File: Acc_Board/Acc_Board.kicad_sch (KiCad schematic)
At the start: 44 parts, among them J1 1053091202, J10 1053091202, J11 1053091202, J12 776087-1, J2 1053091202, J3 1053091202, J4 1053091202, J5 1053091202, J6 1053091202, J9 1053091202, K1 Relay_SPST-NO, U1 ISO1050DUB, U13 R-78B5.0-2.0, U2 NUCLEO-L432KC, U4 PQDE6W-Q110-S5-H-D

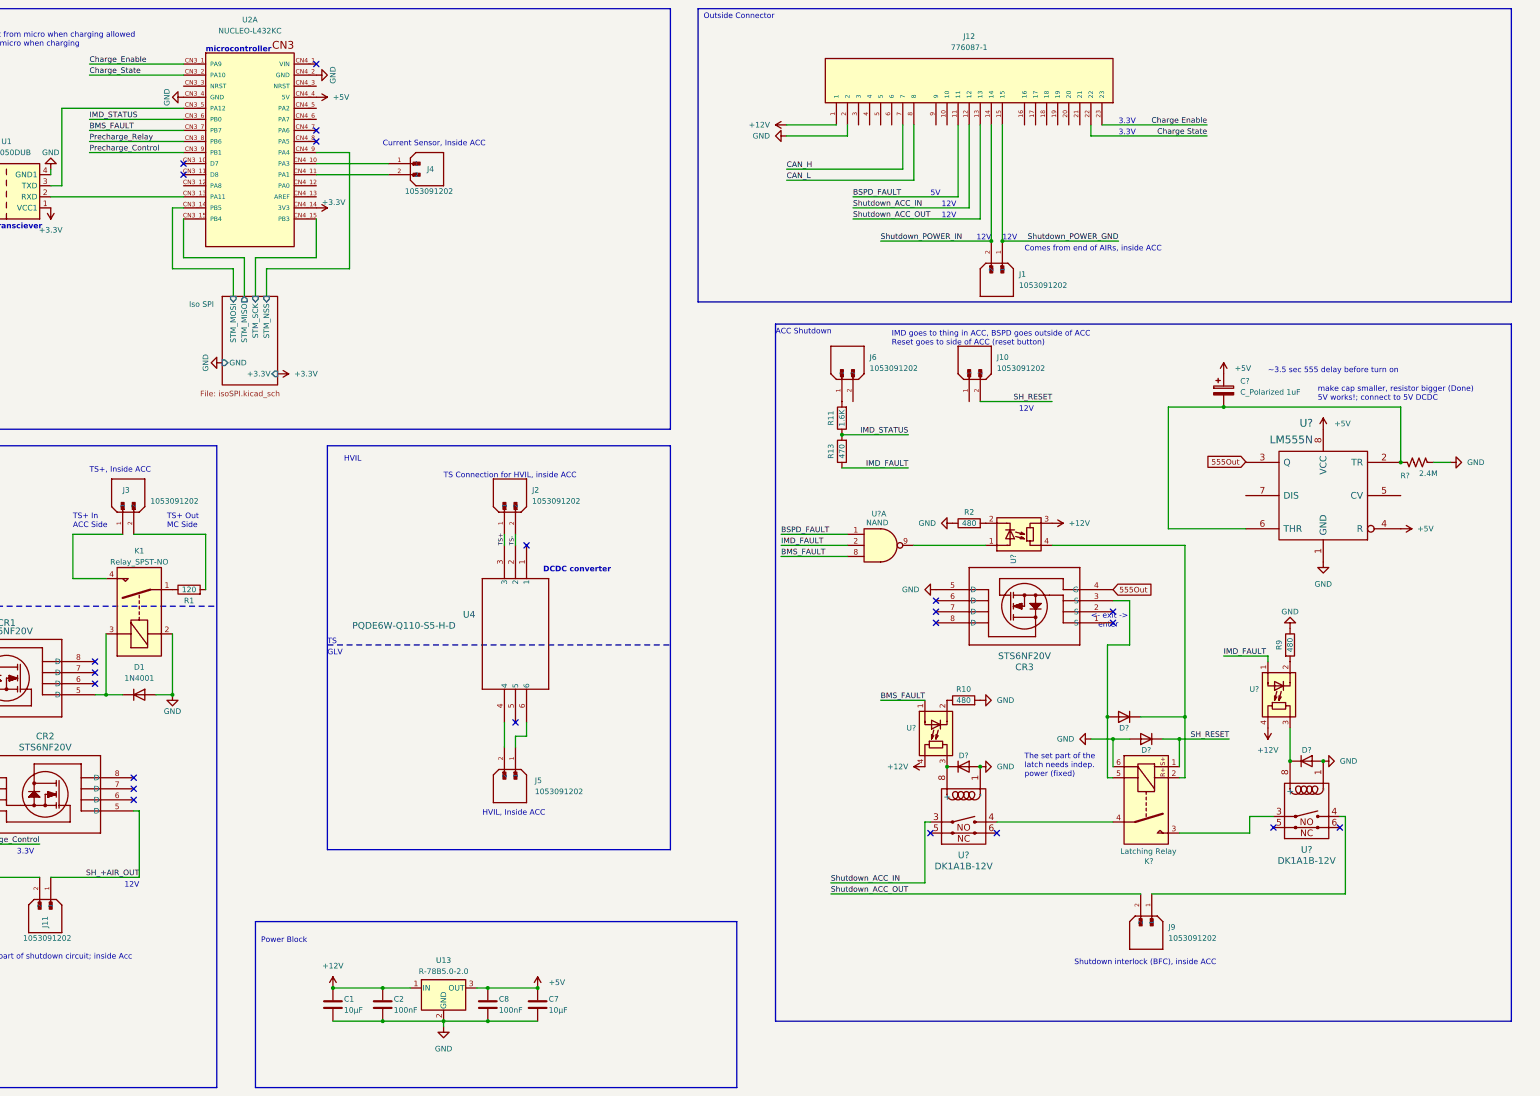
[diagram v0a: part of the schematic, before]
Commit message: Updated shutdown circuit pins in acc board
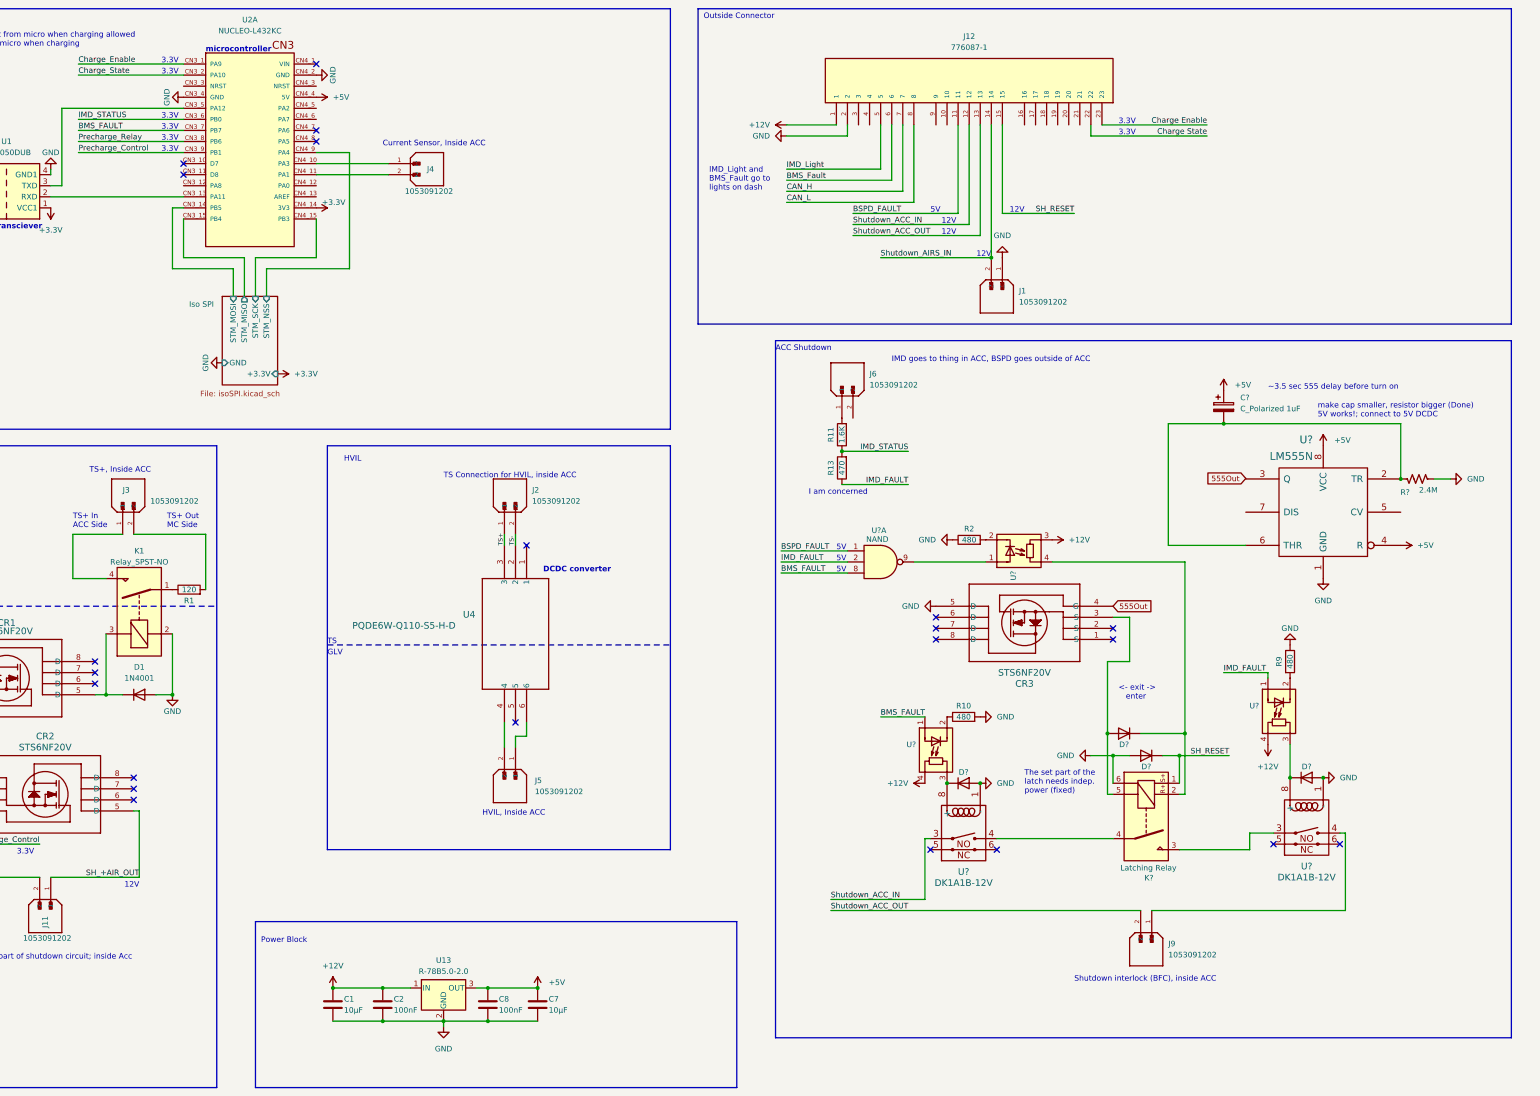
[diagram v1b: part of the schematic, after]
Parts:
- removed J10: 1053091202, 1FS_2_Global_Footprint_Library:MOLEX_1053091202, symbol molex_1053091202:1053091202
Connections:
- net GND: now also J1.1
- net SH_RESET: now also J12.15
- net IMD_Light: now reaches J12.5
- net BMS_Fault: now reaches J12.6
- removed net Shutdown_POWER_GND: J1.1, J12.15
- net Shutdown_POWER_IN renamed Shutdown_AIRS_IN
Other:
- note added: "I am concerned"
- note added: "IMD goes to thing in ACC, BSPD goes outside of ACC"
- note added: "IMD_Light and BMS_Fault go to lights on dash"
- note removed: "Comes from end of AIRs, inside ACC"
- note removed: "IMD goes to thing in ACC, BSPD goes outside of ACC Reset goes to side of ACC (reset button)"
- moved on the sheet: C?, CR3, D?, J1, J6, J9, K?, R10, R11, R13, R2, R9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

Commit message: Worked on Acc Board tracks
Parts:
- C?: value C_Polarized 1uF -> 1µF; footprint Capacitor_THT:CP_Axial_L20.0mm_D10.0mm_P26.00mm_Horizontal -> (none)
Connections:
- net CAN_H: now also J12.8; no longer J12.7
- net CAN_L: now also J12.7; no longer J12.8
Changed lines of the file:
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@@
     (effects (font (size 1.27 1.27)) (justify left bottom))
   )
-  (text "~3.5 sec 555 delay before turn on" (at 345.44 102.87 0)
+  (text "~3.5 sec 555 delay before turn on" (at 342.9 102.87 0)
     (effects (font (size 1.27 1.27)) (justify left bottom))
   )
@@
     (effects (font (size 1.27 1.27)) (justify left bottom))
   )
-  (label "CAN_L" (at 234.95 59.69 0) (fields_autoplaced)
+  (label "CAN_H" (at 234.95 59.69 0) (fields_autoplaced)
     (effects (font (size 1.27 1.27)) (justify left bottom))
   )
@@
     (effects (font (size 1 1)) (justify left bottom))
   )
-  (label "CAN_H" (at 234.95 57.15 0) (fields_autoplaced)
-    (effects (font (size 1.27 1.27)) (justify left bottom))
-  )
   (label "Precharge_Control" (at 63.5 207.01 180) (fields_autoplaced)
     (effects (font (size 1.27 1.27)) (justify right bottom))
   )
   (label "BSPD_FAULT" (at 233.68 139.7 0) (fields_autoplaced)
+    (effects (font (size 1.27 1.27)) (justify left bottom))
+  )
+  (label "CAN_L" (at 234.95 57.15 0) (fields_autoplaced)
     (effects (font (size 1.27 1.27)) (justify left bottom))
   )
@@
       (effects (font (size 1.27 1.27)) (justify left))
     )
-    (property "Value" "C_Polarized 1uF" (at 339.09 107.061 0)
-      (effects (font (size 1.27 1.27)) (justify left))
-    )
-    (property "Footprint" "Capacitor_THT:CP_Axial_L20.0mm_D10.0mm_P26.00mm_Horizontal" (at 336.2452 110.49 0)
-      (effects (font (size 1.27 1.27)) hide)
-    )
+    (property "Value" "1µF" (at 339.09 107.061 0)
+      (effects (font (size 1.27 1.27)) (justify left))
+    )
+    (property "Footprint" "" (at 336.2452 110.49 0)
+      (effects (font (size 1.27 1.27)) hide)
+    )

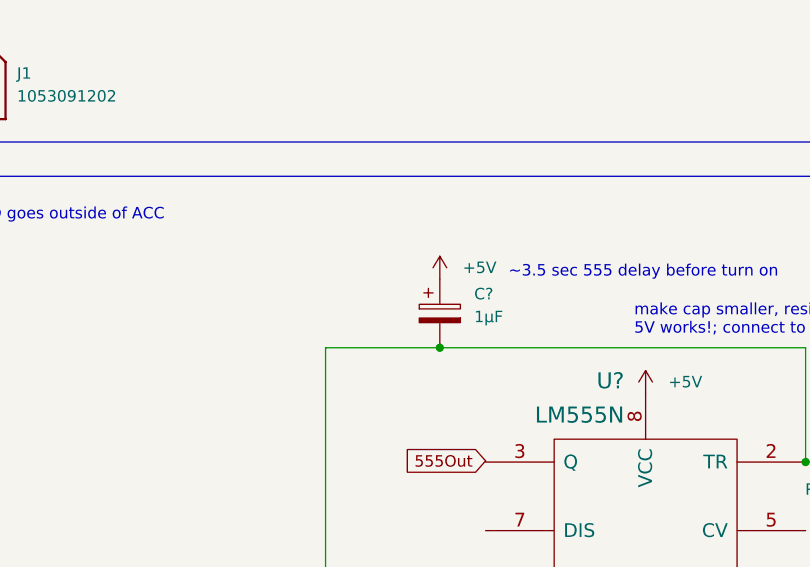
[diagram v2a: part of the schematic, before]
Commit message: fixed 555 capacitors
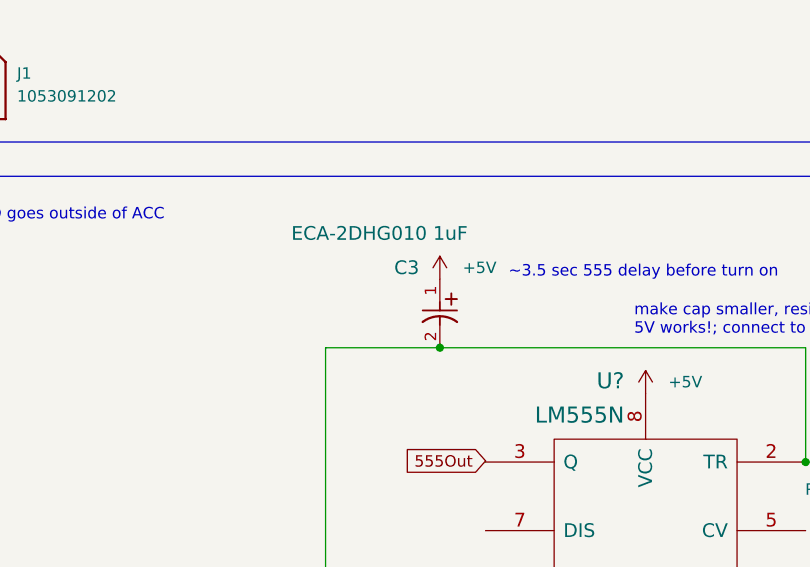
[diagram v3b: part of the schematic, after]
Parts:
- removed C?: 1µF, symbol Device:C_Polarized
- added C3: ECA-2DHG010 1uF, PCAP_63x112_PAN, symbol 1FS_2_Global_Symbol_Library:ECA-2DHG010
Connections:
- net +5V: now also C3.1
- net at R?.1, U?.2 (TR), U?.6 (THR): now also C3.2
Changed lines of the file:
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@@
   (junction (at 166.37 240.03) (diameter 0) (color 0 0 0 0)
   )
+  (junction (at 335.28 110.49) (diameter 0) (color 0 0 0 0)
+  )
   (junction (at 40.64 53.34) (diameter 0) (color 0 0 0 0)
   )
@@
   )
   (junction (at 375.92 123.19) (diameter 0) (color 0 0 0 0)
-  )
-  (junction (at 335.28 110.49) (diameter 0) (color 0 0 0 0)
   )
   (junction (at 326.39 181.61) (diameter 0) (color 0 0 0 0)
@@
     (stroke (width 0) (type default))
   )
-  (wire (pts (xy 335.28 110.49) (xy 375.92 110.49))
-    (stroke (width 0) (type default))
-  )
   (wire (pts (xy 127 72.39) (xy 127 63.5))
     (stroke (width 0) (type default))
@@
   )
   (wire (pts (xy 250.19 64.77) (xy 276.86 64.77))
+    (stroke (width 0) (type default))
+  )
+  (wire (pts (xy 335.28 110.49) (xy 375.92 110.49))
     (stroke (width 0) (type default))
   )
@@
     )
   )
+  (symbol (lib_id "1FS_2_Global_Symbol_Library:ECA-2DHG010") (at 335.28 102.87 270) (unit 1)
+    (in_bom yes) (on_board yes) (dnp no)
+    (property "Reference" "C3" (at 330.2 101.6 90)
+      (effects (font (size 1.524 1.524)) (justify left))
+    )
+    (property "Value" "ECA-2DHG010 1uF" (at 318.77 97.79 90)
+      (effects (font (size 1.524 1.524)) (justify left))
+    )
+    (property "Footprint" "PCAP_63x112_PAN" (at 335.28 102.87 0)
+      (effects (font (size 1.27 1.27) italic) hide)
+    )
+    (property "Datasheet" "ECA-2DHG010" (at 335.28 102.87 0)
+      (effects (font (size 1.27 1.27) italic) hide)
+    )
+    (pin "1")
+    (pin "2")
+    (instances
+      (project "Acc_Board"
+        (path "/e19d26dd-723b-45e6-9d59-b1730158e759"
+          (reference "C3") (unit 1)
+        )
+      )
+    )
+  )
   (symbol (lib_id "power:GND") (at 156.21 248.92 0) (unit 1)
     (in_bom yes) (on_board yes) (dnp no) (fields_autoplaced)
@@
         )
       )
-    )
-  )
-  (symbol (lib_id "Device:C_Polarized") (at 335.28 106.68 0) (unit 1)
-    (in_bom yes) (on_board yes) (dnp no) (fields_autoplaced)
-    (property "Reference" "C?" (at 339.09 104.521 0)
-      (effects (font (size 1.27 1.27)) (justify left))
-    )
-    (property "Value" "1µF" (at 339.09 107.061 0)
-      (effects (font (size 1.27 1.27)) (justify left))
-    )
-    (property "Footprint" "" (at 336.2452 110.49 0)
-      (effects (font (size 1.27 1.27)) hide)
-    )
-    (property "Datasheet" "https://www.digikey.com/en/products/detail/vishay-sprague/TE1135-E3/5612613?s=N4IgjCBcoGwJxVAYygMwIYBsDOBTANCAPZQDaIALGGABxwDsIAuoQA4AuUIAyuwE4BLAHYBzEAF9CAJgAMFBNBApIGHAWJlwMmQAIArQDFmbTpBABVIQPYB5VAFlc6bAFc%2BuCdJn0FyNFjxCEkhyMCkdADVjEA4uS2s7R2c3D0kQAFopRCUofhd1YPIAVmZxNKyQmKJMdEEAL1wAEx0kdFZ0JGsiPh0wbRdUUqA" (at 335.28 106.68 0)
-      (effects (font (size 1.27 1.27)) hide)
-    )
-    (pin "1")
-    (pin "2")
-    (instances
-      (project "BSPD"
-        (path "/9b958334-fa88-4811-8197-71444a07b1b5"
-          (reference "C?") (unit 1)
-        )
-      )
-      (project "Acc_Board"
-        (path "/e19d26dd-723b-45e6-9d59-b1730158e759"
-          (reference "C3") (unit 1)
-        )
-      )
